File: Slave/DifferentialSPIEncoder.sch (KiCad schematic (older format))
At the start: 20 parts, among them J1 8P8C_Shielded, U1 MAX485E, U2 MAX485E, U3 MAX485E, U4 AS5048A

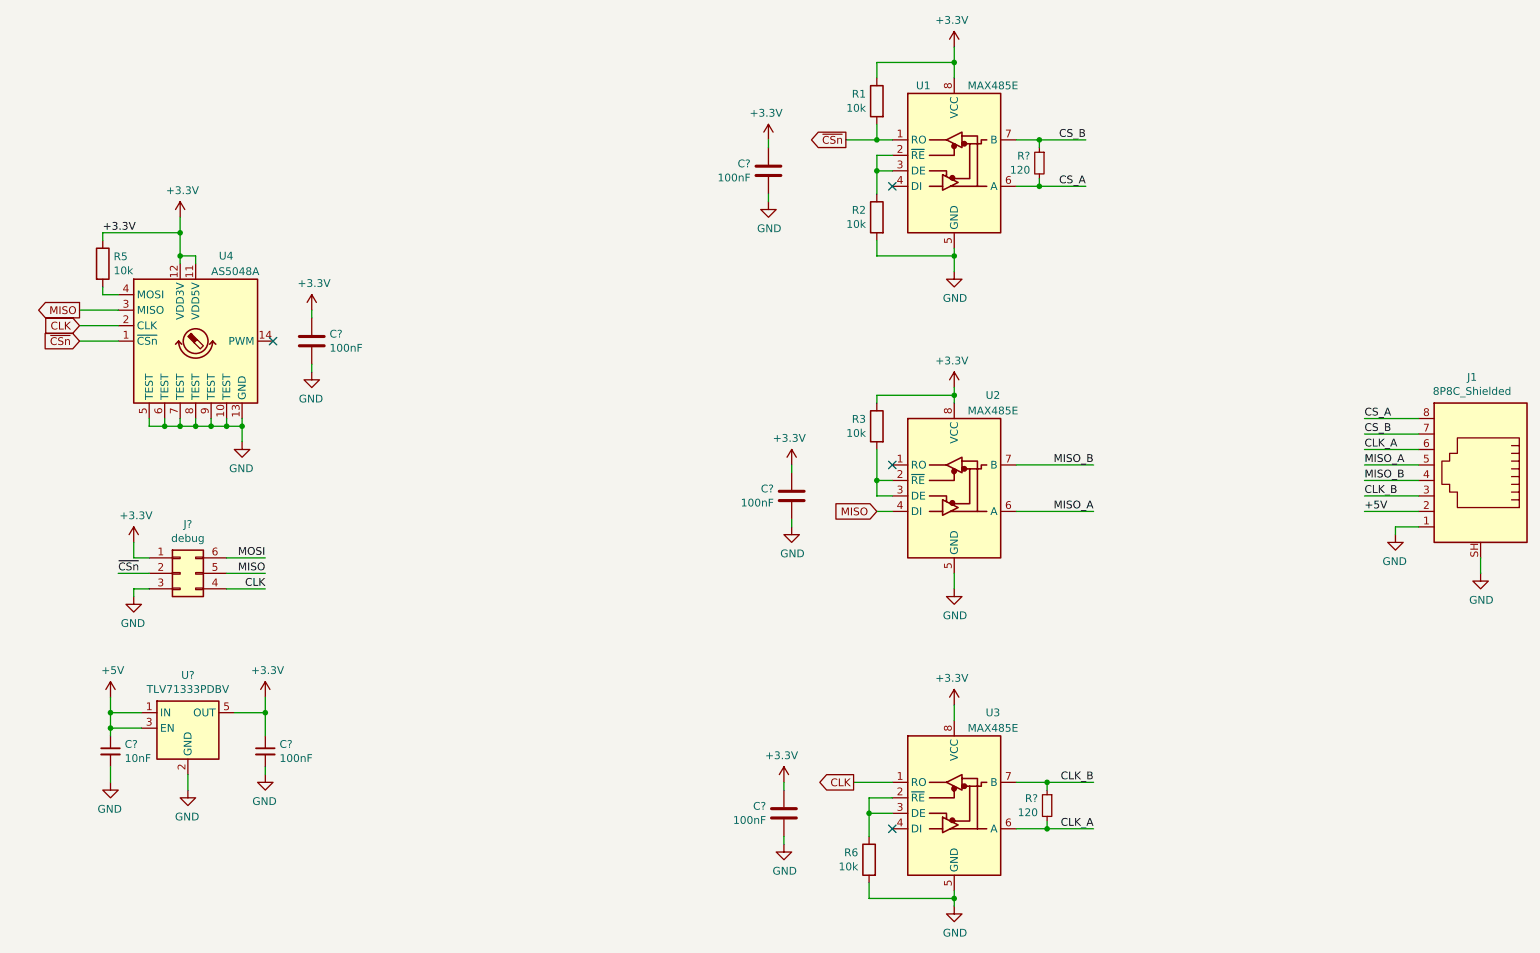
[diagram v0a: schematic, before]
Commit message: Add LPFs to single-ended signals
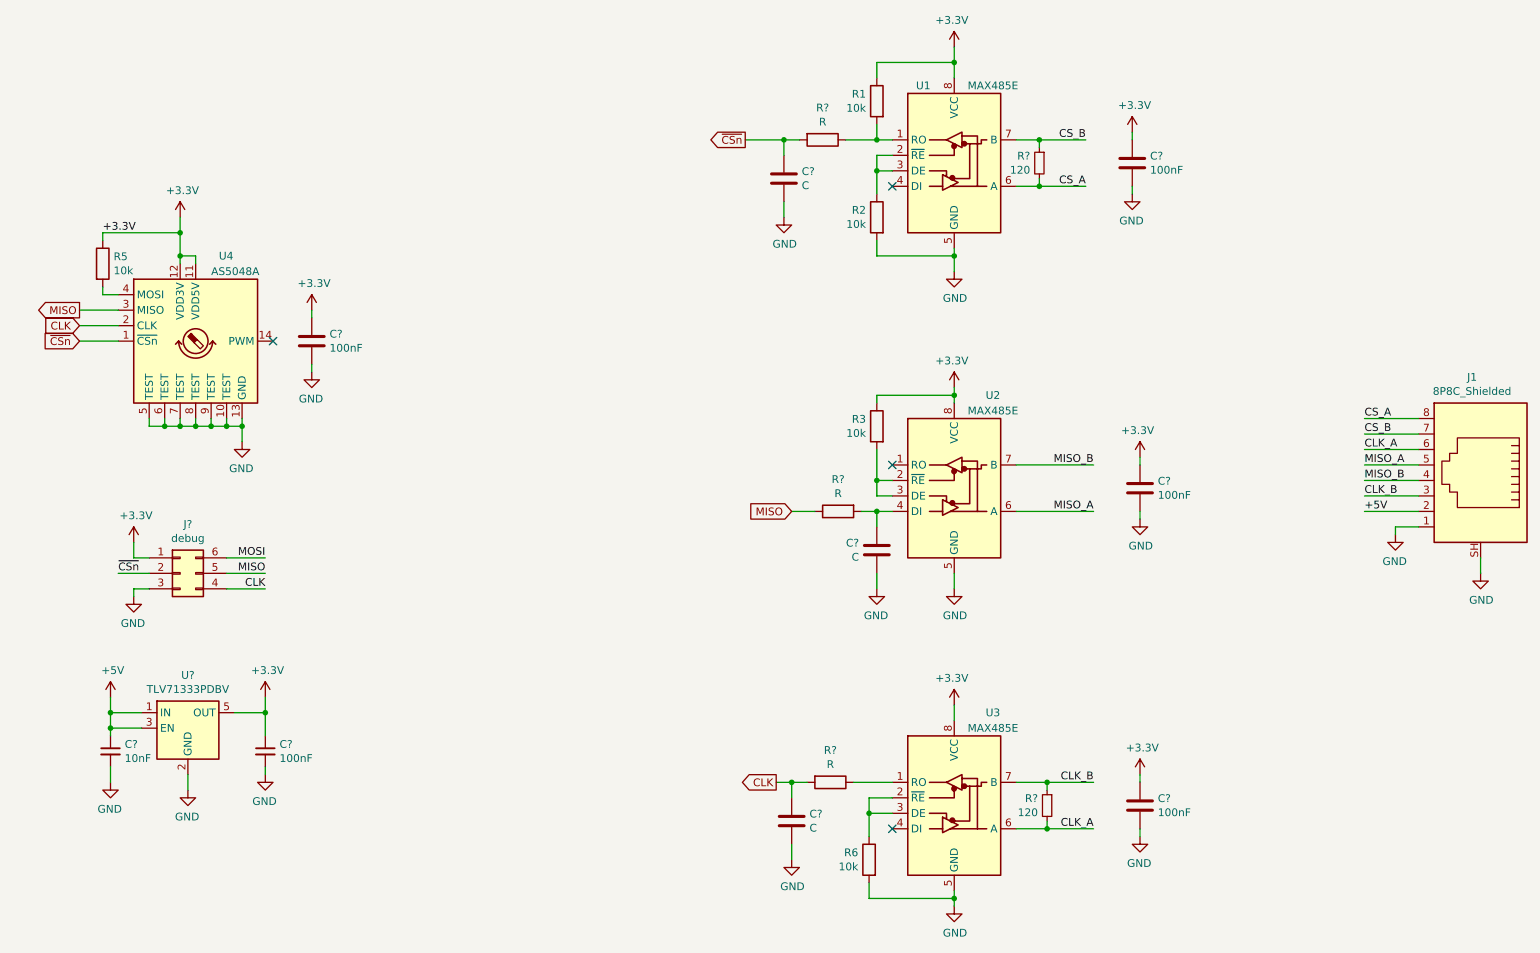
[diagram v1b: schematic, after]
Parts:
- added C? (x3): C, symbol Device:C
- added R? (x3): R, symbol Device:R
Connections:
- net CLK: now also C?.1, R?.2; no longer U3.1 (RO)
- net GND: now also C?.2, C?.2, C?.2
- net MISO: now also R?.1; no longer U2.4 (DI)
- net ~CSn: now also C?.1, R?.2; no longer R1.2, U1.1 (RO)
- new net: R1.2, R?.1, U1.1 (RO)
- new net: C?.1, R?.2, U2.4 (DI)
- new net: R?.1, U3.1 (RO)
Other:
- moved on the sheet: C?

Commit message: Start laying out Master
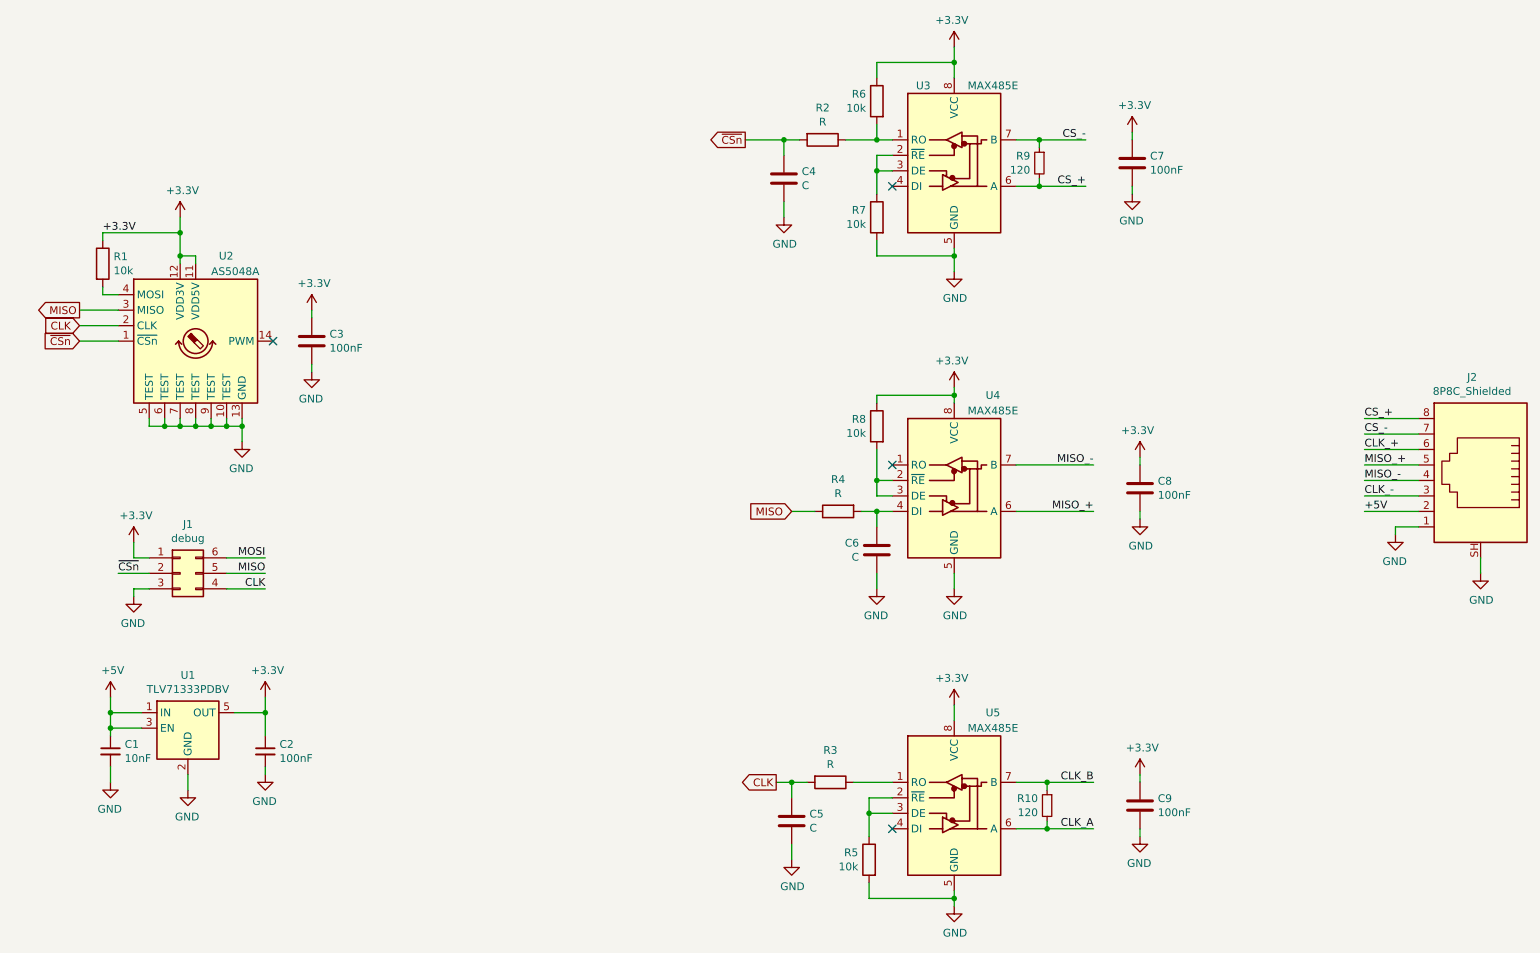
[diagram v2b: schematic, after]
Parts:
- C1, C2, C3, C4, C5, C6, C7, C8, C9: renamed from C?; footprint (none) -> Capacitor_SMD:C_0805_2012Metric_Pad1.15x1.40mm_HandSolder
- J1: renamed from J?; footprint (none) -> Connector_PinSocket_2.54mm:PinSocket_2x03_P2.54mm_Vertical
- J2: renamed from J1; footprint (none) -> Connector_RJ:RJ45_Amphenol_RJHSE5380
- R1: renamed from R5; footprint (none) -> Resistor_SMD:R_0805_2012Metric_Pad1.15x1.40mm_HandSolder
- R10, R2, R3, R4, R9: renamed from R?; footprint (none) -> Resistor_SMD:R_0805_2012Metric_Pad1.15x1.40mm_HandSolder
- R5: renamed from R6; footprint (none) -> Resistor_SMD:R_0805_2012Metric_Pad1.15x1.40mm_HandSolder
- R6: renamed from R1; footprint (none) -> Resistor_SMD:R_0805_2012Metric_Pad1.15x1.40mm_HandSolder
- R7: renamed from R2; footprint (none) -> Resistor_SMD:R_0805_2012Metric_Pad1.15x1.40mm_HandSolder
- R8: renamed from R3; footprint (none) -> Resistor_SMD:R_0805_2012Metric_Pad1.15x1.40mm_HandSolder
- U3: renamed from U1; footprint (none) -> Package_SO:SOIC-8_3.9x4.9mm_P1.27mm
- U4: renamed from U2; footprint (none) -> Package_SO:SOIC-8_3.9x4.9mm_P1.27mm
- U5: renamed from U3; footprint (none) -> Package_SO:SOIC-8_3.9x4.9mm_P1.27mm
- gave numbers to parts that had none: 1
- renumbered U4 to U2
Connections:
- net CLK_A: no longer J2.6
- net CLK_B: no longer J2.3
- net CS_A renamed CS_+
- net CS_B renamed CS_-
- net MISO_A renamed MISO_+
- net MISO_B renamed MISO_-
- new net CLK_+: J2.6
- new net CLK_-: J2.3
